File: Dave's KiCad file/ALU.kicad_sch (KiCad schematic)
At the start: 0 parts

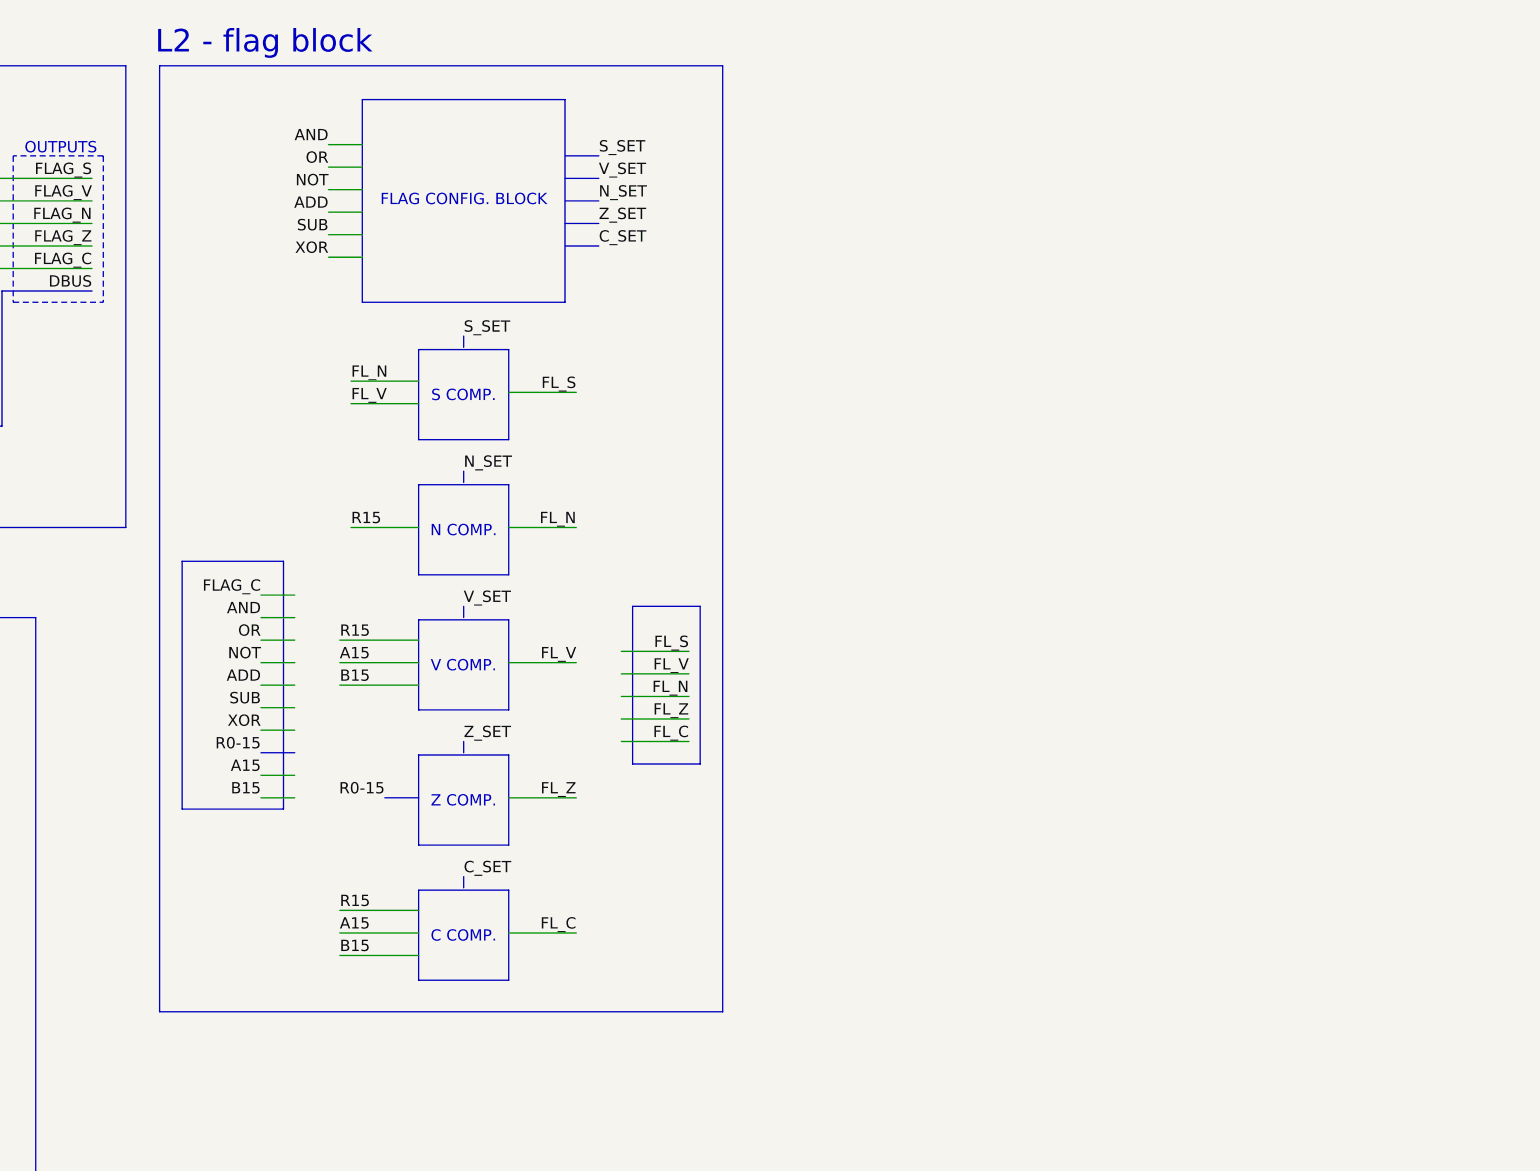
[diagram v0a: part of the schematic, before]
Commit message: Add L3 tree for ALU
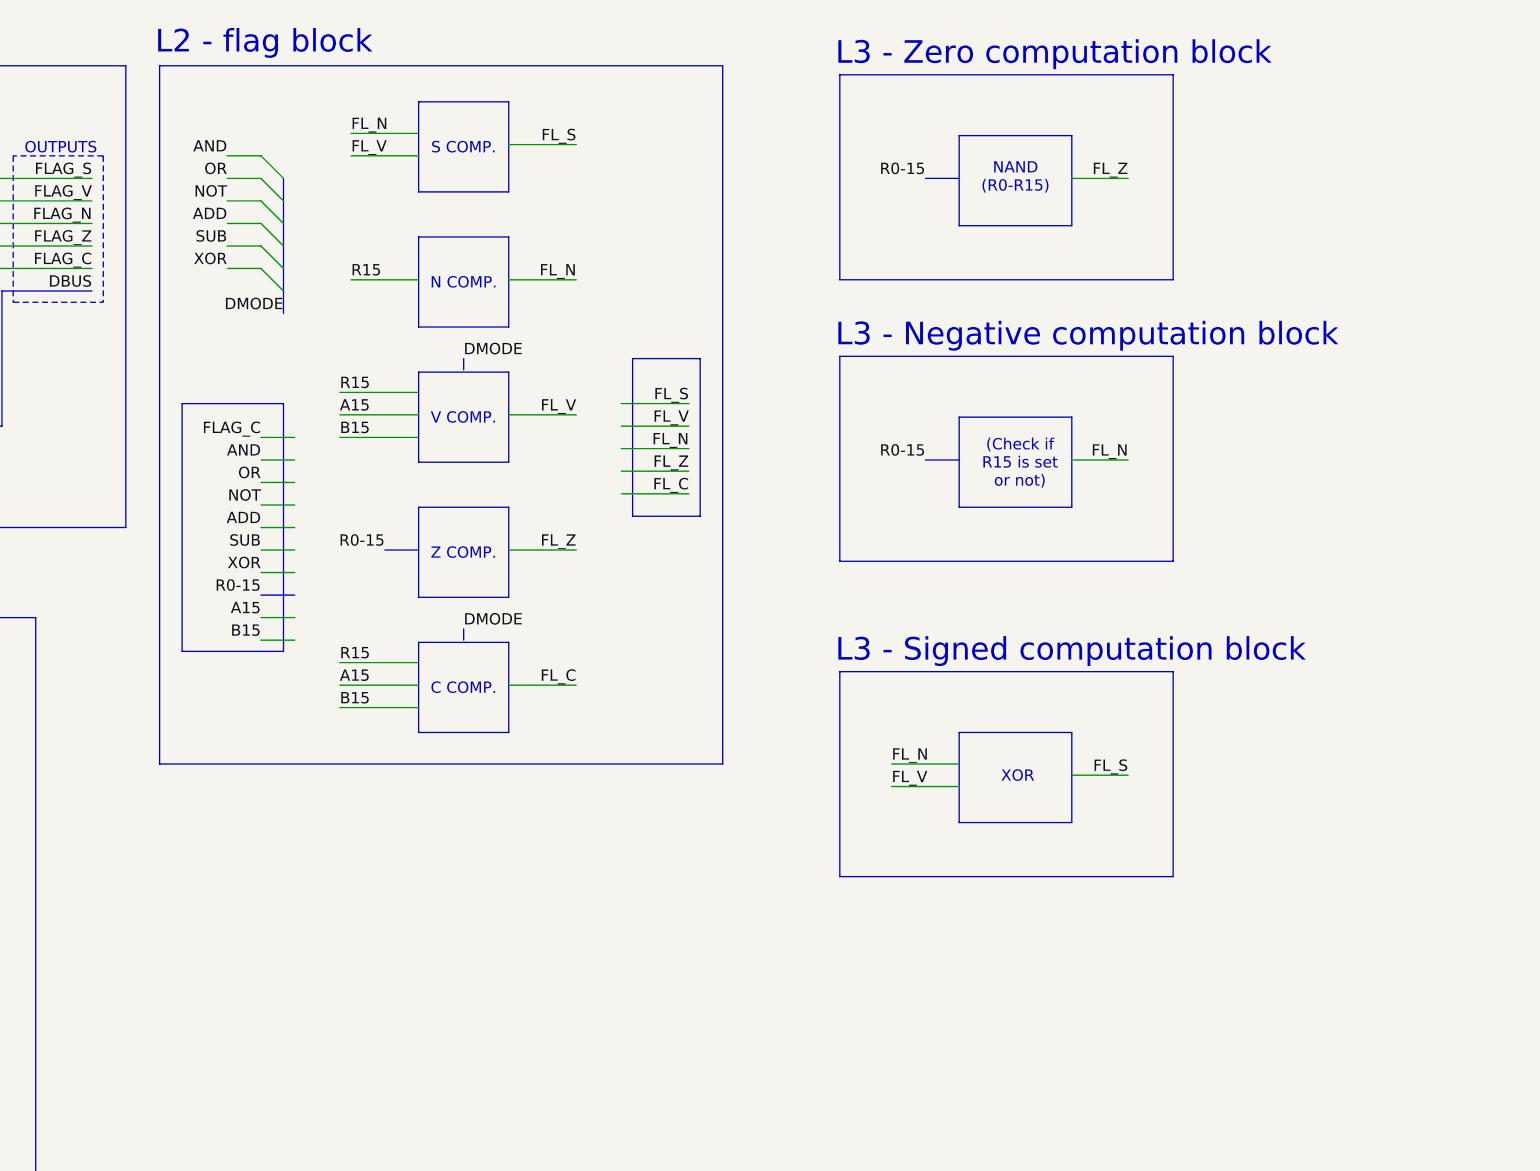
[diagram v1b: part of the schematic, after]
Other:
- note added: "(Check if R15 is set or not)"
- note added: "L3 - Negative computation block"
- note added: "L3 - Signed computation block"
- note added: "L3 - Zero computation block"
- note added: "NAND (R0-R15)"
- note removed: "FLAG CONFIG. BLOCK"

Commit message: Upload the progress
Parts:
- added U1: 74HC373, symbol 74xx:74HC373
- added U2: 74125, symbol 74xx_IEEE:74125
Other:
- note added: "L2 - Latch A"
- note added: "L3 - Carry computation block"
- note added: "L3 - Negative computation block (NO NEED FOR CIRCUIT)"
- note added: "L3 - Overflow computation block"
- note added: "L3 - Signed computation block (NO NEED FOR CIRCUIT)"
- note removed: "L3 - Negative computation block"
- note removed: "L3 - Signed computation block"

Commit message: Update 28/9
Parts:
- removed U1: 74HC373, symbol 74xx:74HC373
- removed U2: 74125, symbol 74xx_IEEE:74125
- added U2, U3: 74HC244, symbol 74xx:74HC244
- added U4, U5: 74HC273, symbol 74xx:74HC273
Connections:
- net READ: now also U5.11 (Cp)
- net SELB: now also U5.1 (~{Mr})
- new net CTRL: U2.1 (1OE), U2.19 (2OE), U3.1 (1OE), U3.19 (2OE)
- new net GND: U2.10 (GND), U3.10 (GND), U4.10 (GND), U5.10 (GND)
- new net VCC: U2.20 (VCC), U3.20 (VCC), U5.20 (VCC)
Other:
- note added: "L2 - Latch"
- note added: "L2 - Tri-state buffer"
- note added: "L2 ALU - Compute result"
- note removed: "L2 - Latch A"
